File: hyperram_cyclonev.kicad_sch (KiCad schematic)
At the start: 57 parts, among them IC1 AP63205WU, IC2 TXB0108PWR, IC3 S26KL128SDABHI020, IC4 W25Q32JVSSIQ_TR, IC5 S27KL0641DABHI020, J1 ASP-122952-01, J2 HDMI_A, J3 Conn_02x10_Odd_Even, J4 Conn_02x10_Odd_Even, J5 Conn_02x06_Odd_Even, J6 Conn_02x06_Odd_Even, J7 Conn_02x06_Odd_Even, Q1 BSS138, Q2 BSS138

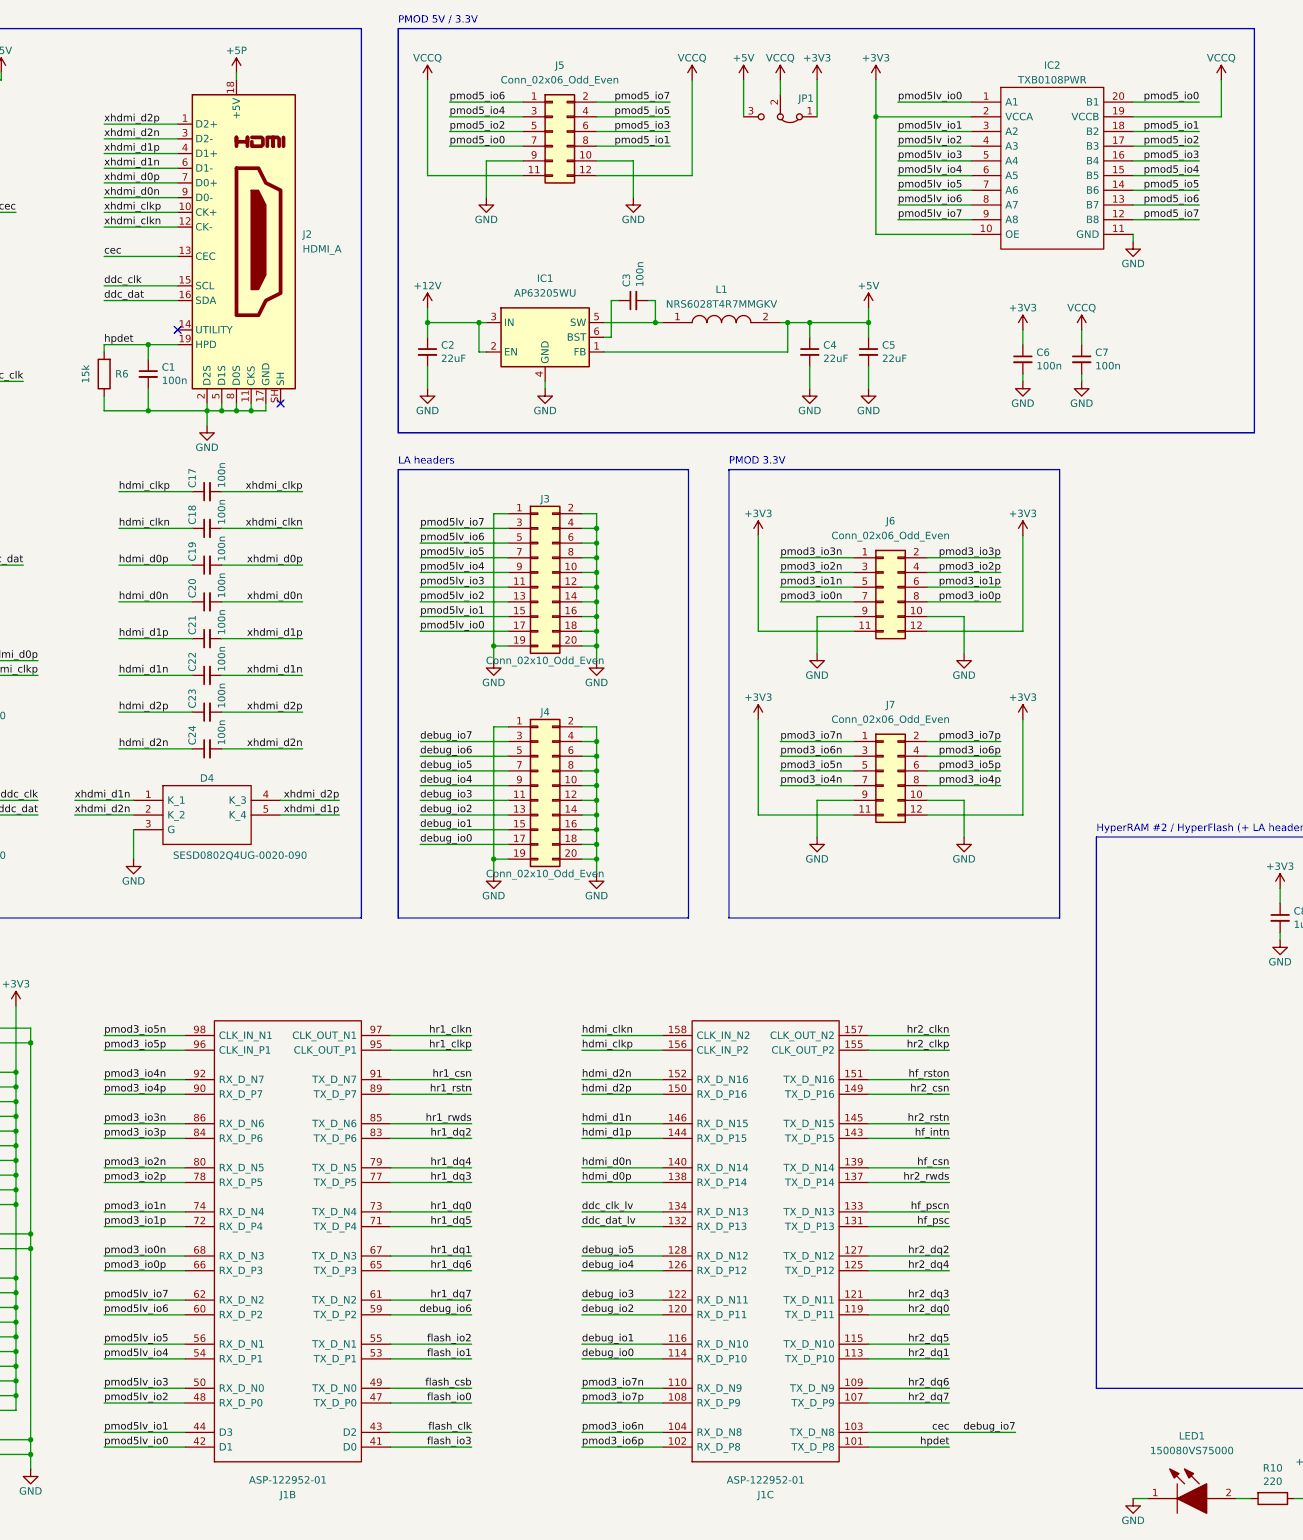
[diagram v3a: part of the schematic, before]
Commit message: Reaarranged signals assignments to simplify routing
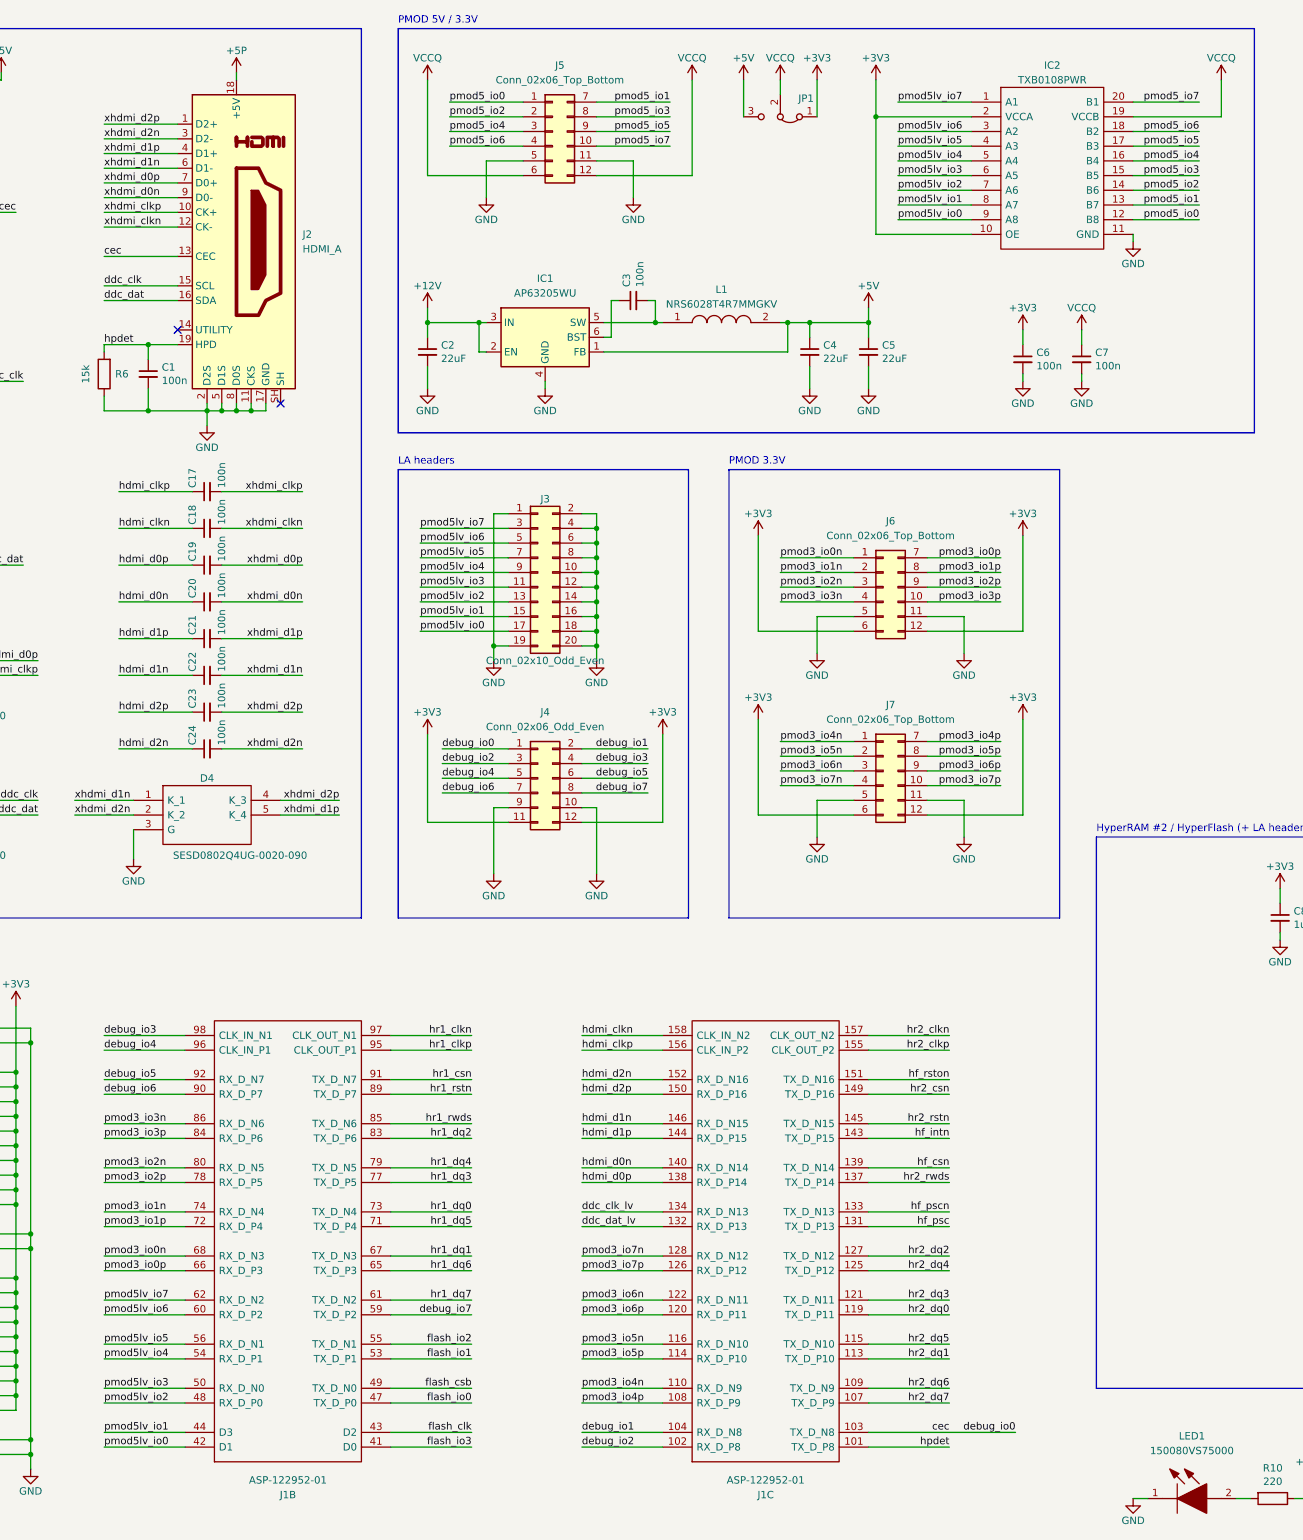
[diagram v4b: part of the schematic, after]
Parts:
- removed J4: Conn_02x10_Odd_Even, Connector_PinHeader_2.54mm:PinHeader_2x10_P2.54mm_Vertical, symbol Connector_Generic:Conn_02x10_Odd_Even
- removed J5, J6, J7: Conn_02x06_Odd_Even, hyperram_cyclonev:610112249221, symbol Connector_Generic:Conn_02x06_Odd_Even
- added J4: Conn_02x06_Odd_Even, Connector_PinHeader_2.54mm:PinHeader_2x06_P2.54mm_Vertical, symbol Connector_Generic:Conn_02x06_Odd_Even
- added J5, J6, J7: Conn_02x06_Top_Bottom, hyperram_cyclonev:610112249221_PMOD_Bottom, symbol Connector_Generic:Conn_02x06_Top_Bottom
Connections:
- net debug_io0 is gone; now on net pmod3_io5p: J1.114 (RX_D_P10)
- net +3V3: now also J4.11 (Pin_11), J4.12 (Pin_12), J6.12 (Pin_12), J6.6 (Pin_6), J7.12 (Pin_12), J7.6 (Pin_6)
- net GND: now also J4.10 (Pin_10), J4.9 (Pin_9), J5.11 (Pin_11), J5.5 (Pin_5), J6.11 (Pin_11), J6.5 (Pin_5), J7.11 (Pin_11), J7.5 (Pin_5)
- net VCCQ: now also J5.12 (Pin_12), J5.6 (Pin_6)
- net cec: now also J4.1 (Pin_1)
- net debug_io1: now also J1.104 (RX_D_N8), J4.2 (Pin_2); no longer J1.116 (RX_D_N10)
- net debug_io2: now also J1.102 (RX_D_P8), J4.3 (Pin_3); no longer J1.120 (RX_D_P11)
- net debug_io3: now also J1.98 (CLK_IN_N1), J4.4 (Pin_4); no longer J1.122 (RX_D_N11)
- net debug_io4: now also J1.96 (CLK_IN_P1), J4.5 (Pin_5); no longer J1.126 (RX_D_P12)
- net debug_io5: now also J1.92 (RX_D_N7), J4.6 (Pin_6); no longer J1.128 (RX_D_N12)
- net debug_io6: now also J1.90 (RX_D_P7), J4.7 (Pin_7); no longer J1.59 (TX_D_P2)
- net pmod3_io0n: now also J6.1 (Pin_1)
- net pmod3_io0p: now also J6.7 (Pin_7)
- net pmod3_io1n: now also J6.2 (Pin_2)
- net pmod3_io1p: now also J6.8 (Pin_8)
- net pmod3_io2n: now also J6.3 (Pin_3)
- net pmod3_io2p: now also J6.9 (Pin_9)
- net pmod3_io3n: now also J6.4 (Pin_4)
- net pmod3_io3p: now also J6.10 (Pin_10)
- net pmod3_io4n: now also J1.110 (RX_D_N9), J7.1 (Pin_1); no longer J1.92 (RX_D_N7)
- net pmod3_io4p: now also J1.108 (RX_D_P9), J7.7 (Pin_7); no longer J1.90 (RX_D_P7)
- net pmod3_io5n: now also J1.116 (RX_D_N10), J7.2 (Pin_2); no longer J1.98 (CLK_IN_N1)
- net pmod3_io5p: now also J7.8 (Pin_8); no longer J1.96 (CLK_IN_P1)
- net pmod3_io6n: now also J1.122 (RX_D_N11), J7.3 (Pin_3); no longer J1.104 (RX_D_N8)
- net pmod3_io6p: now also J1.120 (RX_D_P11), J7.9 (Pin_9); no longer J1.102 (RX_D_P8)
- net pmod3_io7n: now also J1.128 (RX_D_N12), J7.4 (Pin_4); no longer J1.110 (RX_D_N9)
- net pmod3_io7p: now also J1.126 (RX_D_P12), J7.10 (Pin_10); no longer J1.108 (RX_D_P9)
- net pmod5_io0: now also IC2.12 (B8), J5.1 (Pin_1); no longer IC2.20 (B1)
- net pmod5_io1: now also IC2.13 (B7), J5.7 (Pin_7); no longer IC2.18 (B2)
- net pmod5_io2: now also IC2.14 (B6), J5.2 (Pin_2); no longer IC2.17 (B3)
- net pmod5_io3: now also IC2.15 (B5), J5.8 (Pin_8); no longer IC2.16 (B4)
- net pmod5_io4: now also IC2.16 (B4), J5.3 (Pin_3); no longer IC2.15 (B5)
- net pmod5_io5: now also IC2.17 (B3), J5.9 (Pin_9); no longer IC2.14 (B6)
- net pmod5_io6: now also IC2.18 (B2), J5.4 (Pin_4); no longer IC2.13 (B7)
- net pmod5_io7: now also IC2.20 (B1), J5.10 (Pin_10); no longer IC2.12 (B8)
- net pmod5lv_io0: now also IC2.9 (A8); no longer IC2.1 (A1)
- net pmod5lv_io1: now also IC2.8 (A7); no longer IC2.3 (A2)
- net pmod5lv_io2: now also IC2.7 (A6); no longer IC2.4 (A3)
- net pmod5lv_io3: now also IC2.6 (A5); no longer IC2.5 (A4)
- net pmod5lv_io4: now also IC2.5 (A4); no longer IC2.6 (A5)
- net pmod5lv_io5: now also IC2.4 (A3); no longer IC2.7 (A6)
- net pmod5lv_io6: now also IC2.3 (A2); no longer IC2.8 (A7)
- net pmod5lv_io7: now also IC2.1 (A1); no longer IC2.9 (A8)
- new net debug_io7: J1.59 (TX_D_P2), J4.8 (Pin_8)
